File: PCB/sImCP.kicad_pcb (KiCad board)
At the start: 2 copper layers, 155.6 x 140 mm, 79 parts, among them J1 AVR-ISP-6, SW1 RESET, SW2 BOOT, U1 ATmega328P-AU, Y1 16MHz

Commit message: fixed encoders mess, wiring missing
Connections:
- DOB1 pad 11: Net-(DOB1-Pad11) -> (no net)
- DOB1 pad 8: Net-(DOB1-Pad8) -> GND
- J1 pad 3: SCK -> R2B
- RE1 pad A: DOB1B -> MOSI
- RE2 pad A: R1B -> MISO
- RE2 pad B: DOB1A -> R2B
- U1 pad 17: SCK -> R2B
- U1 pad 19: Net-(U1-Pad19) -> (no net)
- U1 pad 20: Net-(U1-Pad20) -> (no net)
- U1 pad 22: Net-(U1-Pad22) -> (no net)
- USB1 pad A8: Net-(USB1-PadA8) -> (no net)
- USB1 pad B8: Net-(USB1-PadB8) -> (no net)
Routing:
- net DOB1B: track 171.8 -> 0.00 mm, vias 2 -> 0
- net DOB1A: track 116.4 -> 0.00 mm, vias 5 -> 0
- net R1B: track 80.8 -> 0.07 mm, vias 3 -> 0
- net R2B: track 0.00 -> 39.8 mm
- net SCK: track 39.4 -> 0.00 mm
- net GND: track 366.9 -> 392.6 mm

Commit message: updated pcb with new routing for the encoders
now using a set of pins for each encoder instead of the shared model
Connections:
- DOB1 pad 11: (no net) -> Net-(DOB1-Pad11)
- U1 pad 19: (no net) -> Net-(U1-Pad19)
- U1 pad 20: (no net) -> Net-(U1-Pad20)
- U1 pad 22: (no net) -> Net-(U1-Pad22)
- USB1 pad A8: (no net) -> Net-(USB1-PadA8)
- USB1 pad B8: (no net) -> Net-(USB1-PadB8)
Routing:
- net DOB1A: track 0.00 -> 99.8 mm, vias 0 -> 2
- net DOB1B: track 0.00 -> 85.1 mm, vias 0 -> 1
- net R1B: track 0.07 -> 72.8 mm, vias 0 -> 3
- net MISO: track 41.0 -> 108.8 mm, vias 0 -> 1
- net MOSI: track 48.9 -> 114.4 mm, vias 1 -> 4
- net R2B: track 39.8 -> 104.8 mm, vias 0 -> 4
- net GND: track 392.6 -> 386.1 mm, vias 10 -> 12

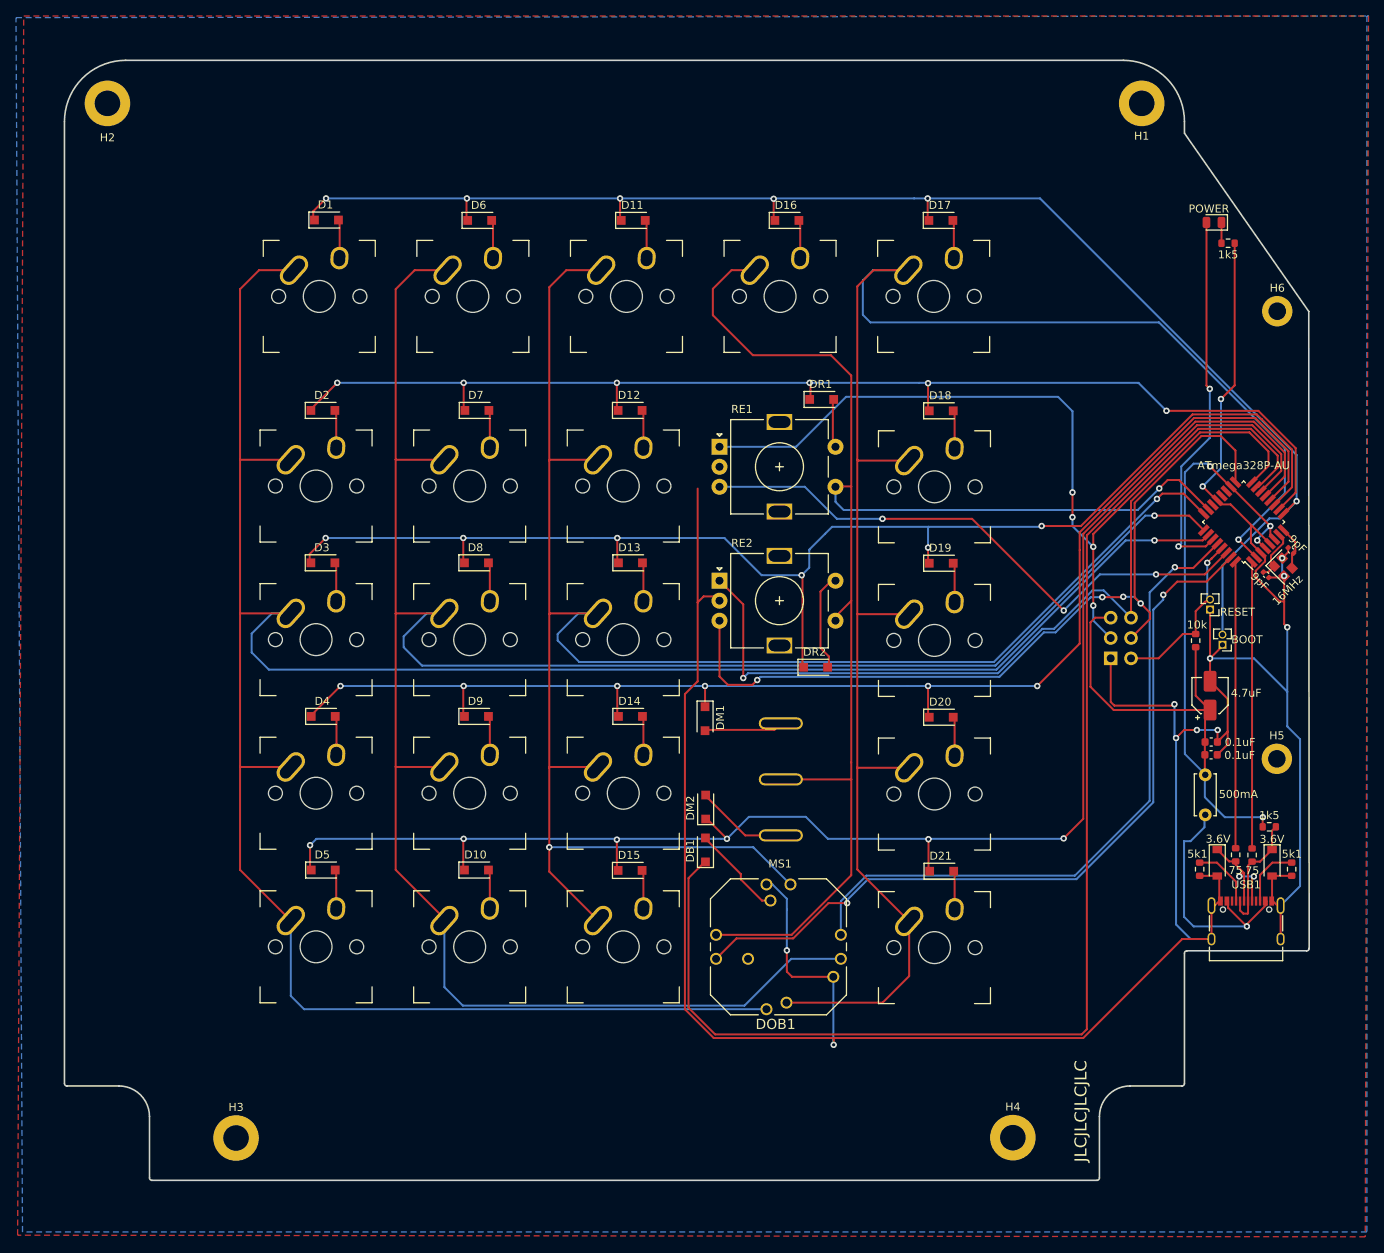
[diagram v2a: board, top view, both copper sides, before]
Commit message: [FAB FILES] feat: changed 4u7 capacitor to THT
Changed capacitor to THT as previous part number has no stock
Regenerated fabrication files
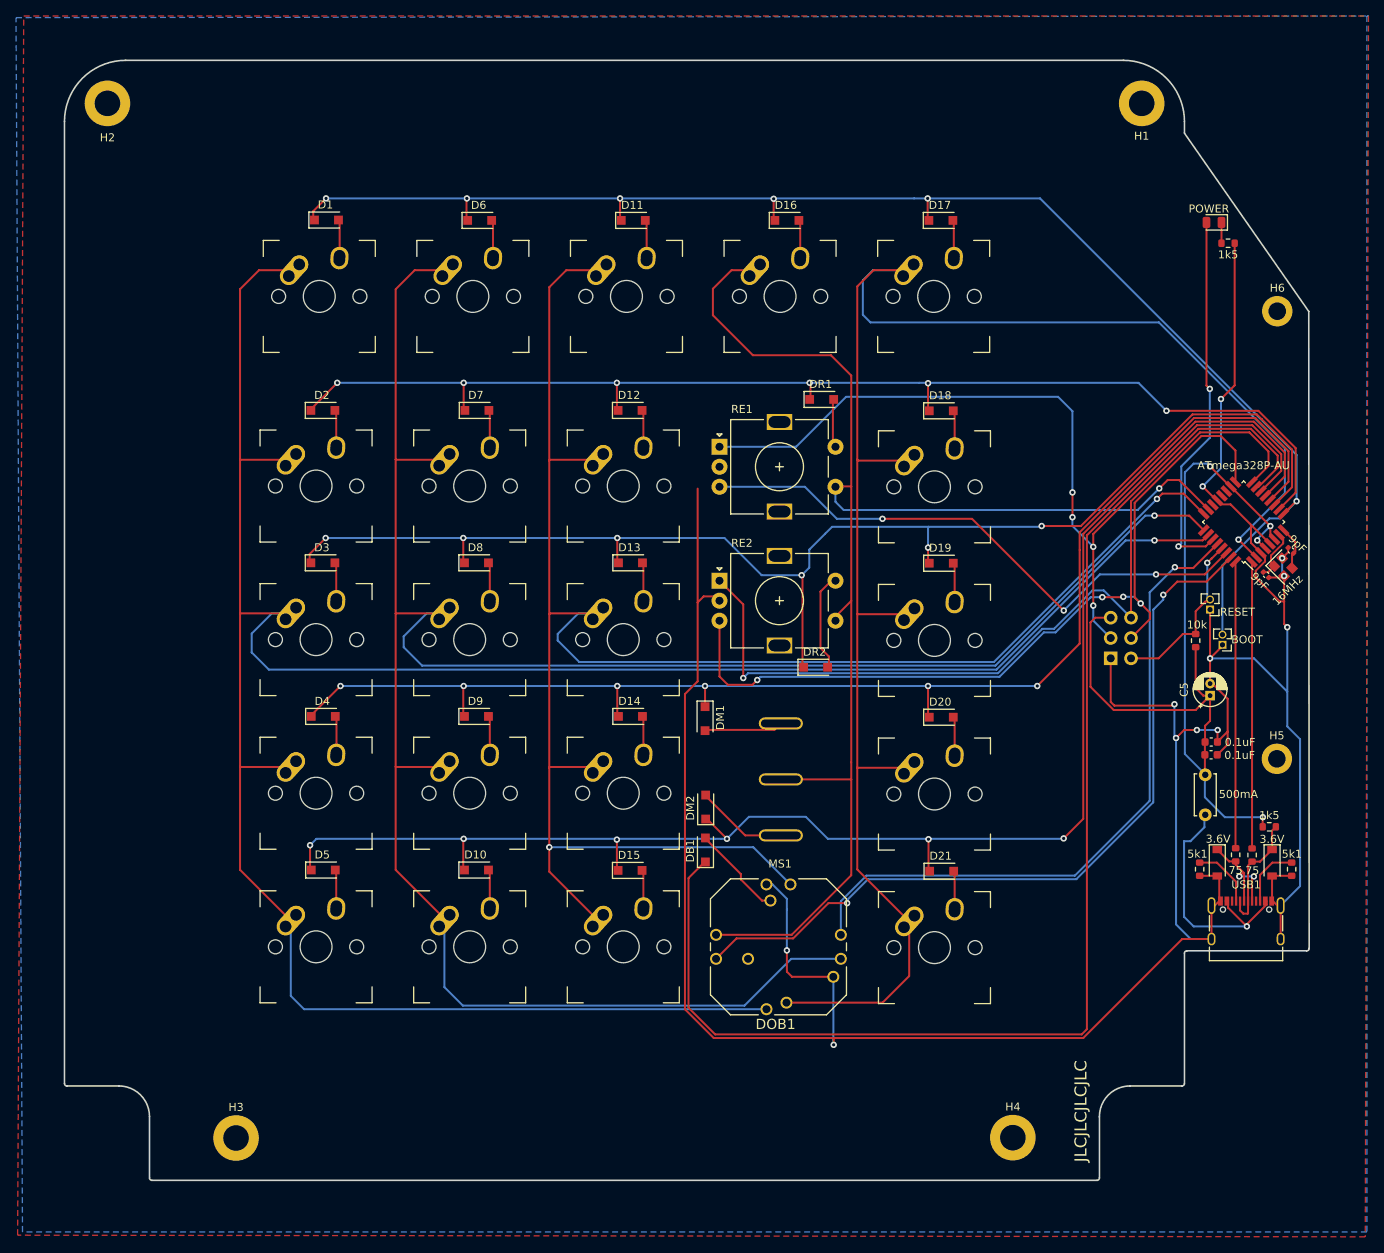
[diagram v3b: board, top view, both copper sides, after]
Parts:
- C5: footprint Capacitor_SMD:CP_Elec_4x5.3 -> Capacitor_THT:CP_Radial_D4.0mm_P1.50mm
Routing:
- net +5V: track 115.3 -> 116.6 mm
